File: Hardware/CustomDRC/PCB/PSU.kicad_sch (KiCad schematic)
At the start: 0 parts

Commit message: Update - finished schematic for revision A
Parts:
- added C201: 0u1, Capacitor_SMD:C_0603_1608Metric_Pad1.08x0.95mm_HandSolder, symbol Device:C_Small
- added C202, C203: 10u, Capacitor_SMD:C_1206_3216Metric_Pad1.33x1.80mm_HandSolder, symbol Device:C_Small
- added C204, C205: 22u, Capacitor_SMD:C_0805_2012Metric_Pad1.18x1.45mm_HandSolder, symbol Device:C_Small
- added C206, C207: 2u2, Capacitor_SMD:C_0805_2012Metric_Pad1.18x1.45mm_HandSolder, symbol Device:C_Small
- added D201: 1N4148WS, Diode_SMD:D_SOD-323_HandSoldering, symbol Device:D_Schottky_Small
- added D202: US1M, Diode_SMD:D_SMA_Handsoldering, symbol Device:D_Schottky_Small
- added F201: 2A TRIP, Fuse:Fuse_1206_3216Metric_Pad1.42x1.75mm_HandSolder, symbol Device:Fuse_Small
- added F202: 1A TRIP, Fuse:Fuse_0603_1608Metric_Pad1.05x0.95mm_HandSolder, symbol Device:Fuse_Small
- added L201: 4u7, Inductor_SMD:L_Chilisin_BMRA00040420, symbol Device:L_Small
- added R201: 0R, Resistor_SMD:R_0603_1608Metric_Pad0.98x0.95mm_HandSolder, symbol Device:R_Small
- added TP201, TP202, TP203, TP204: TestPoint_Small, TestPoint:TestPoint_Pad_D1.5mm, symbol Connector:TestPoint_Small
- added U201: AP63205WU-7, Package_TO_SOT_SMD:TSOT-23-6, symbol Regulator_Switching:AP63205WU
- added U202: TLV76733DRVR, Package_SON:WSON-6-1EP_2x2mm_P0.65mm_EP1x1.6mm_ThermalVias, symbol Regulator_Linear:TLV76733DRVx
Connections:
- net DC_IN: now also F201.1
- new net: C202.1, C203.1, D202.1 (K), TP204.1, U201.2 (EN), U201.3 (IN)
- new net: D202.2 (A), F201.2
- new net: C207.2, D201.2 (A), F202.1, U202.1 (OUT), U202.2 (SNS)
- new net: F202.2, R201.1
- new net: C201.2, L201.1, U201.5 (SW)
- new net: C201.1, U201.6 (BST)
- new net +5V: C204.1, C205.1, C206.1, D201.1 (K), L201.2, TP203.1, U201.1 (FB), U202.4 (EN), U202.6 (IN)
- new net GND: C202.2, C203.2, C204.2, C205.2, C206.2, C207.1, TP201.1, TP202.1, U201.4 (GND), U202.3 (GND), U202.5 (GND), U202.7 (PAD)
- new net VCC: R201.2
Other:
- note added: "ADDED 0R TO AVOID VIA ON LAYOUT"
- note added: "CIN RMS >= 3A USE CERAMIC WITH LOW ESR"
- note added: "COUT CERAMIC"
- note added: "DC IN IS PROTECTED UPSTREAM BY MOV AND DAMPING CAPS 100V RATED"
- note added: "ISAT >= 3A R < 100mR FOR EFFICIENCY"
- note added: "OVERCURRENT"
- note added: "PSU 3.3V/1A OUT"
- note added: "PSU 32V IN MAX 5V/2A OUT 1.1MHZ Fswitch"
- note added: "RPP"
- note added: "SWITCHING"
- note added: "THERMALS: I = 250mA V = 5 - 3.3 = 1.7V P = 0.425W Rj = 92.3C/W TEMP: 39.23C + AMB SO SHOULD BE FINE"
- company: (none) -> JS HW
- title: (none) -> CDRC - Custom DRC for Audison AC Link

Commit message: Sync HW changes for V1 PCB
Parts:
- removed C206, C207: 2u2, Capacitor_SMD:C_0805_2012Metric_Pad1.18x1.45mm_HandSolder, symbol Device:C_Small
- removed D201: 1N4148WS, Diode_SMD:D_SOD-323_HandSoldering, symbol Device:D_Schottky_Small
- removed F202: 1A TRIP, Fuse:Fuse_0603_1608Metric_Pad1.05x0.95mm_HandSolder, symbol Device:Fuse_Small
- removed TP202: TestPoint_Small, TestPoint:TestPoint_Pad_D1.5mm, symbol Connector:TestPoint_Small
- removed U202: TLV76733DRVR, Package_SON:WSON-6-1EP_2x2mm_P0.65mm_EP1x1.6mm_ThermalVias, symbol Regulator_Linear:TLV76733DRVx
- F201: value 2A TRIP -> BSMD1206-025-33V
- L201: footprint Inductor_SMD:L_Chilisin_BMRA00040420 -> Inductor_SMD:L_Cenker_CKCS4030; LCSC C5307591 -> C96899; MPN XR0420-4R7M -> SWPA4030S3R9MT; Manufacturer XR -> Sunlord
- U201: value AP63205WU-7 -> AP63203WU-7; LCSC C2071056 -> C780769; MPN AP63205WU-7 -> AP63203WU-7
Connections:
- net +5V is gone; now on net VCC: C204.1, C205.1, L201.2, TP203.1, U201.1 (FB)
- net VCC: now also R201.1
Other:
- note added: "0R 1A RATED 2A OVERLOAD SO ACTS AS FUSE"
- note added: "250mA HOLD 0.5A TRIP"
- note added: "3V3 @ 2A = 6.6W MAX ESP32 @ 250mA NOM = 0.83W ESP32 @ 500mA MAX = 1.65W"
- note added: "PSU 32V IN MAX 3.3V/2A OUT 1.1MHZ Fswitch"
- note removed: "ADDED 0R TO AVOID VIA ON LAYOUT"
- note removed: "PSU 3.3V/1A OUT"
- note removed: "PSU 32V IN MAX 5V/2A OUT 1.1MHZ Fswitch"
- note removed: "THERMALS: I = 250mA V = 5 - 3.3 = 1.7V P = 0.425W Rj = 92.3C/W TEMP: 39.23C + AMB SO SHOULD BE FINE"
- moved on the sheet: C201, C202, C203, C204, C205, D202, F201, L201, TP201, TP203, TP204, U201

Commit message: Updated value of L201 from 4u7 to 3u9
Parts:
- L201: value 4u7 -> 3u9
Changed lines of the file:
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@@
 			)
 		)
-		(property "Value" "4u7"
+		(property "Value" "3u9"
 			(at 179.07 80.772 90)
 			(effects

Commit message: Sync before making breaking changes to RS485 comms protocl and method
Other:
- title: CDRC - Custom DRC for Audison AC Link -> CDRC - Custom DRC for Bit 10D
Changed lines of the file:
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@@
 	(paper "A4")
 	(title_block
-		(title "CDRC - Custom DRC for Audison AC Link")
-		(date "03-09-2024")
-		(rev "A")
+		(title "CDRC - Custom DRC for Bit 10D")
+		(date "01-11-2024")
+		(rev "B")
 		(company "JS HW")
 	)

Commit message: Sync changes to Rev B HW
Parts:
- removed TP201: TestPoint_Small, TestPoint:TestPoint_Pad_D1.5mm, symbol Connector:TestPoint_Small
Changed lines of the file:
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@@
-	)
-	(junction
-		(at 95.25 101.6)
-		(diameter 0)
-		(color 0 0 0 0)
 	)
 	(junction
@@
 	(wire
 		(pts
-			(xy 88.9 101.6) (xy 95.25 101.6)
+			(xy 93.98 101.6) (xy 133.35 101.6)
 		)
 		(stroke
@@
 	(wire
 		(pts
-			(xy 95.25 102.87) (xy 95.25 101.6)
-		)
-		(stroke
-			(width 0)
-			(type default)
-		)
-	)
-	(wire
-		(pts
-			(xy 88.9 101.6) (xy 88.9 102.87)
+			(xy 93.98 101.6) (xy 93.98 102.87)
 		)
 		(stroke
@@
 		(pts
 			(xy 133.35 101.6) (xy 138.43 101.6)
-		)
-		(stroke
-			(width 0)
-			(type default)
-		)
-	)
-	(wire
-		(pts
-			(xy 95.25 101.6) (xy 133.35 101.6)
 		)
 		(stroke
@@
 	)
 	(symbol
-		(lib_id "Connector:TestPoint_Small")
-		(at 95.25 102.87 180)
-		(unit 1)
-		(exclude_from_sim no)
-		(in_bom no)
-		(on_board yes)
-		(dnp no)
-		(property "Reference" "TP201"
-			(at 98.298 104.394 0)
-			(effects
-				(font
-					(size 1.27 1.27)
-				)
-				(justify left)
-			)
-		)
-		(property "Value" "TestPoint_Small"
-			(at 93.98 101.6001 0)
-			(effects
-				(font
-					(size 1.27 1.27)
-				)
-				(justify left)
-				(hide yes)
-			)
-		)
-		(property "Footprint" "TestPoint:TestPoint_Pad_D1.5mm"
-			(at 90.17 102.87 0)
-			(effects
-				(font
-					(size 1.27 1.27)
-				)
-				(hide yes)
-			)
-		)
-		(property "Datasheet" "~"
-			(at 90.17 102.87 0)
-			(effects
-				(font
-					(size 1.27 1.27)
-				)
-				(hide yes)
-			)
-		)
-		(property "Description" "test point"
-			(at 95.25 102.87 0)
-			(effects
-				(font
-					(size 1.27 1.27)
-				)
-				(hide yes)
-			)
-		)
-		(property "Manufacturer" ""
-			(at 95.25 102.87 0)
-			(effects
-				(font
-					(size 1.27 1.27)
-				)
-				(hide yes)
-			)
-		)
-		(pin "1"
-		)
-		(instances
-			(project "CDRC"
-				(path "/77fe34f2-8fb9-443a-b963-d96f8958fb53/b65e5f69-768f-4a28-b5d1-2ae9c8049607"
-					(reference "TP201")
-					(unit 1)
-				)
-			)
-		)
-	)
-	(symbol
 		(lib_id "Device:R_Small")
 		(at 222.25 91.44 90)
@@
 	(symbol
 		(lib_id "power:GND")
-		(at 88.9 102.87 0)
+		(at 93.98 102.87 0)
 		(unit 1)
 		(exclude_from_sim no)
@@
 		(dnp no)
 		(property "Reference" "#PWR0201"
-			(at 88.9 109.22 0)
+			(at 93.98 109.22 0)
 			(effects
 				(font
@@
 		)
 		(property "Value" "GND"
-			(at 88.9 106.68 0)
+			(at 93.98 106.68 0)
 			(effects
 				(font
@@
 		)
 		(property "Footprint" ""
-			(at 88.9 102.87 0)
+			(at 93.98 102.87 0)
 			(effects
 				(font
@@
 		)
 		(property "Datasheet" ""
-			(at 88.9 102.87 0)
+			(at 93.98 102.87 0)
 			(effects
 				(font
@@
 		)
 		(property "Description" "Power symbol creates a global label with name \"GND\" , ground"
-			(at 88.9 102.87 0)
-			(effects
-				(font
+			(at 93.98 102.87 0)
+			(effects
+				(font

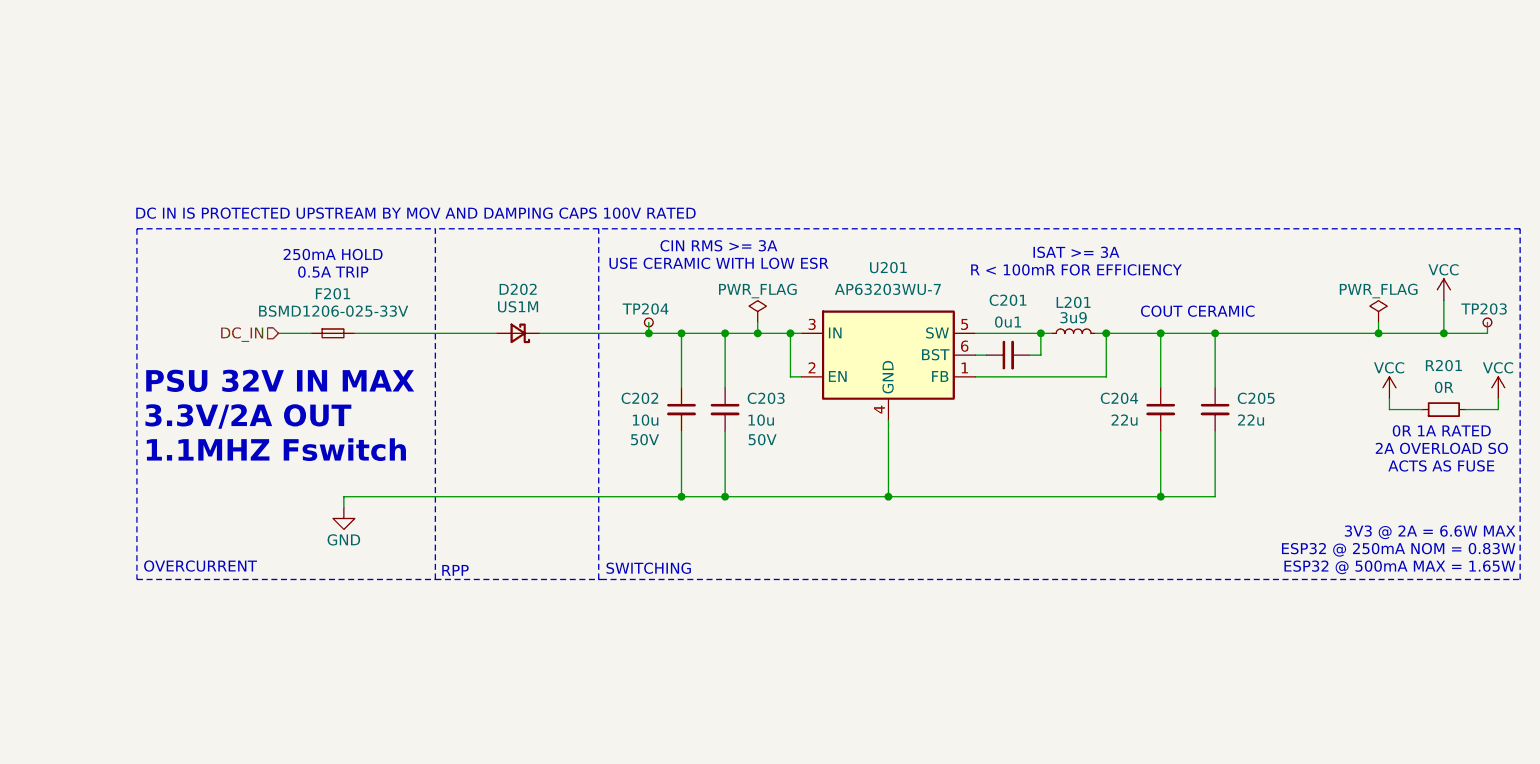
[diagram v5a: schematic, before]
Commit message: Added board renders and PDF plots
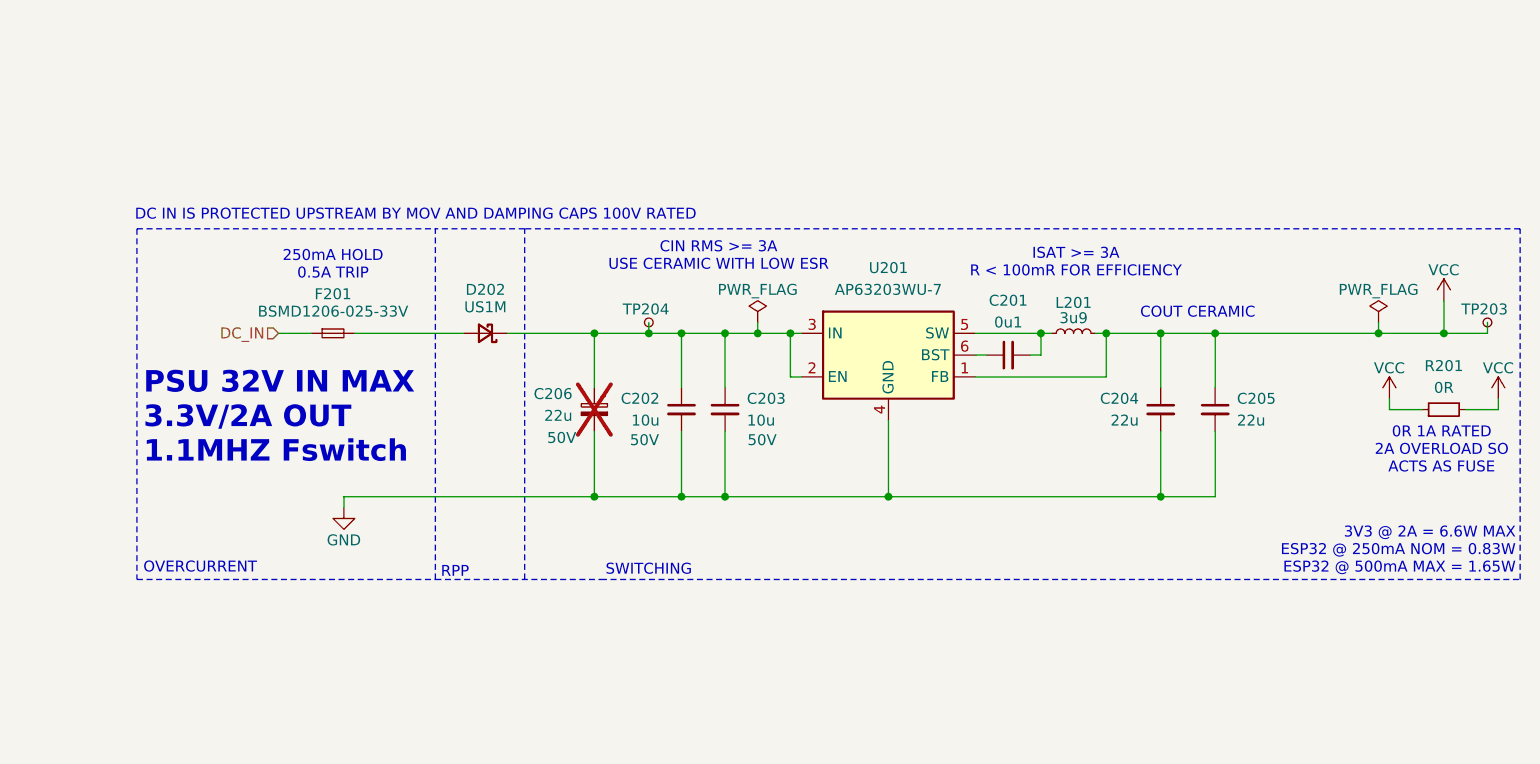
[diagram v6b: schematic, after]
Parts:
- added C206: 22u, Capacitor_SMD:CP_Elec_6.3x5.4_Nichicon, symbol Device:C_Polarized_Small
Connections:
- net GND: now also C206.2
- net at C202.1, C203.1, D202.1 (K)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: now also C206.1
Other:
- moved on the sheet: D202
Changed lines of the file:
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@@
+	)
+	(junction
+		(at 123.19 82.55)
+		(diameter 0)
+		(color 0 0 0 0)
+	)
+	(junction
+		(at 123.19 101.6)
+		(diameter 0)
+		(color 0 0 0 0)
 	)
 	(junction
@@
 	(wire
 		(pts
-			(xy 93.98 101.6) (xy 133.35 101.6)
+			(xy 93.98 101.6) (xy 123.19 101.6)
 		)
 		(stroke
@@
 		)
 	)
+	(wire
+		(pts
+			(xy 123.19 101.6) (xy 133.35 101.6)
+		)
+		(stroke
+			(width 0)
+			(type default)
+		)
+	)
 	(polyline
 		(pts
@@
 	(wire
 		(pts
-			(xy 116.84 82.55) (xy 129.54 82.55)
+			(xy 113.03 82.55) (xy 123.19 82.55)
 		)
 		(stroke
@@
 	(wire
 		(pts
-			(xy 95.25 82.55) (xy 111.76 82.55)
+			(xy 95.25 82.55) (xy 107.95 82.55)
 		)
 		(stroke
@@
 		)
 	)
+	(wire
+		(pts
+			(xy 123.19 82.55) (xy 129.54 82.55)
+		)
+		(stroke
+			(width 0)
+			(type default)
+		)
+	)
 	(polyline
 		(pts
@@
 	(polyline
 		(pts
-			(xy 123.698 111.252) (xy 123.698 70.358)
+			(xy 115.062 111.252) (xy 115.062 70.358)
 		)
 		(stroke
@@
 	(polyline
 		(pts
-			(xy 123.698 70.358) (xy 104.648 70.358)
+			(xy 115.062 70.358) (xy 104.648 70.358)
 		)
 		(stroke
@@
 	(polyline
 		(pts
-			(xy 231.14 70.358) (xy 123.698 70.358)
+			(xy 231.14 70.358) (xy 115.062 70.358)
 		)
 		(stroke
@@
 	(wire
 		(pts
+			(xy 123.19 93.98) (xy 123.19 101.6)
+		)
+		(stroke
+			(width 0)
+			(type default)
+		)
+	)
+	(wire
+		(pts
 			(xy 167.64 87.63) (xy 182.88 87.63)
 		)
@@
 		(pts
 			(xy 133.35 101.6) (xy 138.43 101.6)
+		)
+		(stroke
+			(width 0)
+			(type default)
+		)
+	)
+	(wire
+		(pts
+			(xy 123.19 88.9) (xy 123.19 82.55)
 		)
 		(stroke
@@
 	(symbol
 		(lib_id "Device:D_Schottky_Small")
-		(at 114.3 82.55 180)
+		(at 110.49 82.55 180)
 		(unit 1)
 		(exclude_from_sim no)
@@
 		(dnp no)
 		(property "Reference" "D202"
-			(at 114.3 77.47 0)
+			(at 110.49 77.47 0)
 			(effects
 				(font
@@
 		)
 		(property "Value" "US1M"
-			(at 114.3 79.502 0)
+			(at 110.49 79.502 0)
 			(effects
 				(font
@@
 		)
 		(property "Footprint" "Diode_SMD:D_SMA_Handsoldering"
-			(at 114.3 82.55 90)
+			(at 110.49 82.55 90)
 			(effects
 				(font
@@
 		)
 		(property "Datasheet" "~"
-			(at 114.3 82.55 90)
+			(at 110.49 82.55 90)
 			(effects
 				(font
@@
 		)
 		(property "Description" "Schottky diode, small symbol"
-			(at 114.3 82.55 0)
+			(at 110.49 82.55 0)
 			(effects
 				(font
@@
 		)
 		(property "LCSC" "C412437"
-			(at 114.3 82.55 0)
+			(at 110.49 82.55 0)
 			(effects
 				(font
@@
 		)
 		(property "MPN" "US1M"
-			(at 114.3 82.55 0)
+			(at 110.49 82.55 0)
 			(effects
 				(font
@@
 		)
 		(property "Manufacturer" "MDD(Microdiode Semiconductor)"
-			(at 114.3 82.55 0)
+			(at 110.49 82.55 0)
 			(effects
 				(font
@@
 					(unit 1)
 				)
+			)
+		)
+	)
+	(symbol
+		(lib_id "Device:C_Polarized_Small")
+		(at 123.19 91.44 0)
+		(mirror y)
+		(unit 1)
+		(exclude_from_sim no)
+		(in_bom no)
+		(on_board yes)
+		(dnp yes)
+		(property "Reference" "C206"
+			(at 120.65 89.6239 0)
+			(effects
+				(font
+					(size 1.27 1.27)
+				)
+				(justify left)
+			)
+		)
+		(property "Value" "22u"
+			(at 120.65 92.1639 0)
+			(effects
+				(font
+					(size 1.27 1.27)
+				)
+				(justify left)
+			)
+		)
+		(property "Footprint" "Capacitor_SMD:CP_Elec_6.3x5.4_Nichicon"
+			(at 123.19 91.44 0)
+			(effects
+				(font
+					(size 1.27 1.27)
+				)
+				(hide yes)
+			)
+		)
+		(property "Datasheet" "~"
+			(at 123.19 91.44 0)
+			(effects
+				(font
+					(size 1.27 1.27)
+				)
+				(hide yes)
+			)
+		)
+		(property "Description" "Polarized capacitor, small symbol"
+			(at 123.19 91.44 0)
+			(effects
+				(font
+					(size 1.27 1.27)
+				)
+				(hide yes)
+			)
+		)
+		(property "Voltage Rating" "50V"
+			(at 119.38 94.742 0)
+			(effects
+				(font
+					(size 1.27 1.27)
+					(color 255 0 255 1)
+				)
+			)
+		)
+		(pin "2"
+		)
+		(pin "1"
+		)
+		(instances
+			(project ""
+				(path "/77fe34f2-8fb9-443a-b963-d96f8958fb53/b65e5f69-768f-4a28-b5d1-2ae9c8049607"
+					(reference "C206")
+					(unit 1)
+				)

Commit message: Update HW folder with latest work on rev B
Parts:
- C206: value 22u -> 100U; footprint Capacitor_SMD:CP_Elec_6.3x5.4_Nichicon -> CDRC_Footprints:Capacitor_D6.3xL12mm_SMD; LCSC (none) -> C160200; MPN (none) -> ERZ1HM101E12OT; Manufacturer (none) -> AISHI(Aihua Group); now fitted; now in the parts list
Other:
- note added: "C206 MOUNTED AS SMD INSTEAD OF THROUG-HOLE"
- moved on the sheet: D202
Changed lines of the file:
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@@
 	(title_block
 		(title "CDRC - Custom DRC for Bit 10D")
-		(date "01-11-2024")
+		(date "25-11-2024")
 		(rev "B")
 		(company "JS HW")
@@
 	(polyline
 		(pts
-			(xy 69.85 70.358) (xy 104.648 70.358)
+			(xy 69.85 70.358) (xy 104.394 70.358)
 		)
 		(stroke
@@
 	(polyline
 		(pts
-			(xy 69.85 111.252) (xy 104.648 111.252)
+			(xy 69.85 111.252) (xy 104.394 111.252)
 		)
 		(stroke
@@
 	(polyline
 		(pts
-			(xy 104.648 111.252) (xy 104.648 70.358)
+			(xy 104.394 111.252) (xy 104.394 70.358)
 		)
 		(stroke
@@
 	(polyline
 		(pts
-			(xy 104.648 111.252) (xy 123.952 111.252)
+			(xy 104.394 111.252) (xy 123.952 111.252)
 		)
 		(stroke
@@
 	(wire
 		(pts
-			(xy 113.03 82.55) (xy 123.19 82.55)
+			(xy 111.76 82.55) (xy 123.19 82.55)
 		)
 		(stroke
@@
 	(wire
 		(pts
-			(xy 95.25 82.55) (xy 107.95 82.55)
+			(xy 95.25 82.55) (xy 106.68 82.55)
 		)
 		(stroke
@@
 	(polyline
 		(pts
-			(xy 115.062 70.358) (xy 104.648 70.358)
+			(xy 115.062 70.358) (xy 104.394 70.358)
 		)
 		(stroke
@@
 				(color 255 0 255 1)
 			)
+		)
+	)
+	(text "C206 MOUNTED AS SMD \nINSTEAD OF THROUG-HOLE"
+		(exclude_from_sim no)
+		(at 116.84 105.41 0)
+		(effects
+			(font
+				(size 1.27 1.27)
+				(color 255 0 255 1)
+			)
+			(justify left)
 		)
 	)
@@
 	(symbol
 		(lib_id "Device:D_Schottky_Small")
-		(at 110.49 82.55 180)
+		(at 109.22 82.55 180)
 		(unit 1)
 		(exclude_from_sim no)
@@
 		(dnp no)
 		(property "Reference" "D202"
-			(at 110.49 77.47 0)
+			(at 109.22 77.47 0)
 			(effects
 				(font
@@
 		)
 		(property "Value" "US1M"
-			(at 110.49 79.502 0)
+			(at 109.22 79.502 0)
 			(effects
 				(font
@@
 		)
 		(property "Footprint" "Diode_SMD:D_SMA_Handsoldering"
-			(at 110.49 82.55 90)
+			(at 109.22 82.55 90)
 			(effects
 				(font
@@
 		)
 		(property "Datasheet" "~"
-			(at 110.49 82.55 90)
+			(at 109.22 82.55 90)
 			(effects
 				(font
@@
 		)
 		(property "Description" "Schottky diode, small symbol"
-			(at 110.49 82.55 0)
+			(at 109.22 82.55 0)
 			(effects
 				(font
@@
 		)
 		(property "LCSC" "C412437"
-			(at 110.49 82.55 0)
+			(at 109.22 82.55 0)
 			(effects
 				(font
@@
 		)
 		(property "MPN" "US1M"
-			(at 110.49 82.55 0)
+			(at 109.22 82.55 0)
 			(effects
 				(font
@@
 		)
 		(property "Manufacturer" "MDD(Microdiode Semiconductor)"
-			(at 110.49 82.55 0)
+			(at 109.22 82.55 0)
 			(effects
 				(font
@@
 		(unit 1)
 		(exclude_from_sim no)
-		(in_bom no)
+		(in_bom yes)
 		(on_board yes)
-		(dnp yes)
+		(dnp no)
 		(property "Reference" "C206"
-			(at 120.65 89.6239 0)
+			(at 120.65 90.17 0)
 			(effects
 				(font
@@
 			)
 		)
-		(property "Value" "22u"
-			(at 120.65 92.1639 0)
+		(property "Value" "100U"
+			(at 120.65 92.456 0)
 			(effects
 				(font
@@
 			)
 		)
-		(property "Footprint" "Capacitor_SMD:CP_Elec_6.3x5.4_Nichicon"
+		(property "Footprint" "CDRC_Footprints:Capacitor_D6.3xL12mm_SMD"
 			(at 123.19 91.44 0)
 			(effects
@@
 			)
 		)
+		(property "MPN" "ERZ1HM101E12OT"
+			(at 123.19 91.44 0)
+			(effects
+				(font
+					(size 1.27 1.27)
+				)
+				(hide yes)
+			)
+		)
+		(property "Manufacturer" "AISHI(Aihua Group)"
+			(at 123.19 91.44 0)
+			(effects
+				(font
+					(size 1.27 1.27)
+				)
+				(hide yes)
+			)
+		)
+		(property "LCSC" "C160200"
+			(at 123.19 91.44 0)
+			(effects
+				(font
+					(size 1.27 1.27)
+				)
+				(hide yes)
+			)
+		)
